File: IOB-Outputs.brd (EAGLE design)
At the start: 20.3 x 50.8 mm, 27 parts, among them CON1 CONNECTOR-IO4STD, Q1 MOSFET-N, Q10 MOSFET-P, Q11 MOSFET-P, Q12 MOSFET-P, Q2 MOSFET-N, Q3 MOSFET-N, Q4 MOSFET-N, Q5 MOSFET-N, Q6 MOSFET-N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

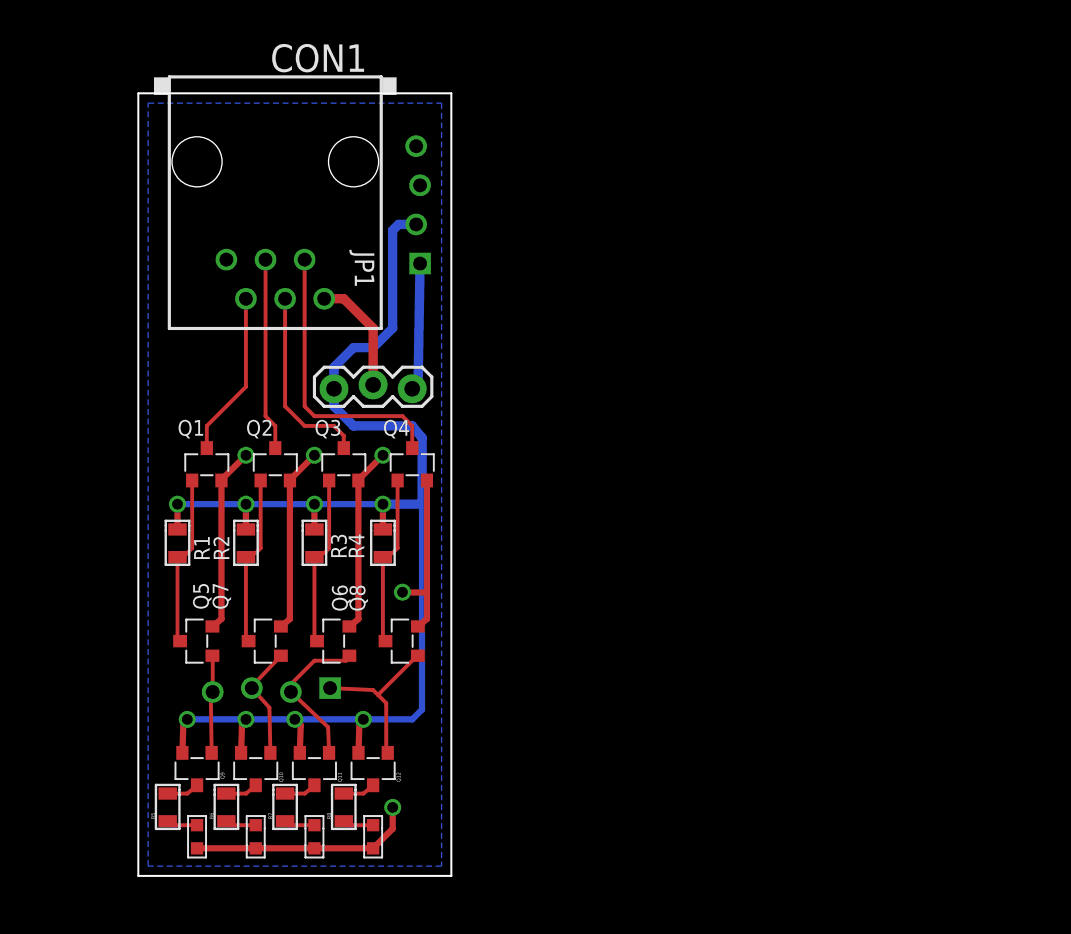
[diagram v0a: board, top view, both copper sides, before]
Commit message: updated to new IOB design
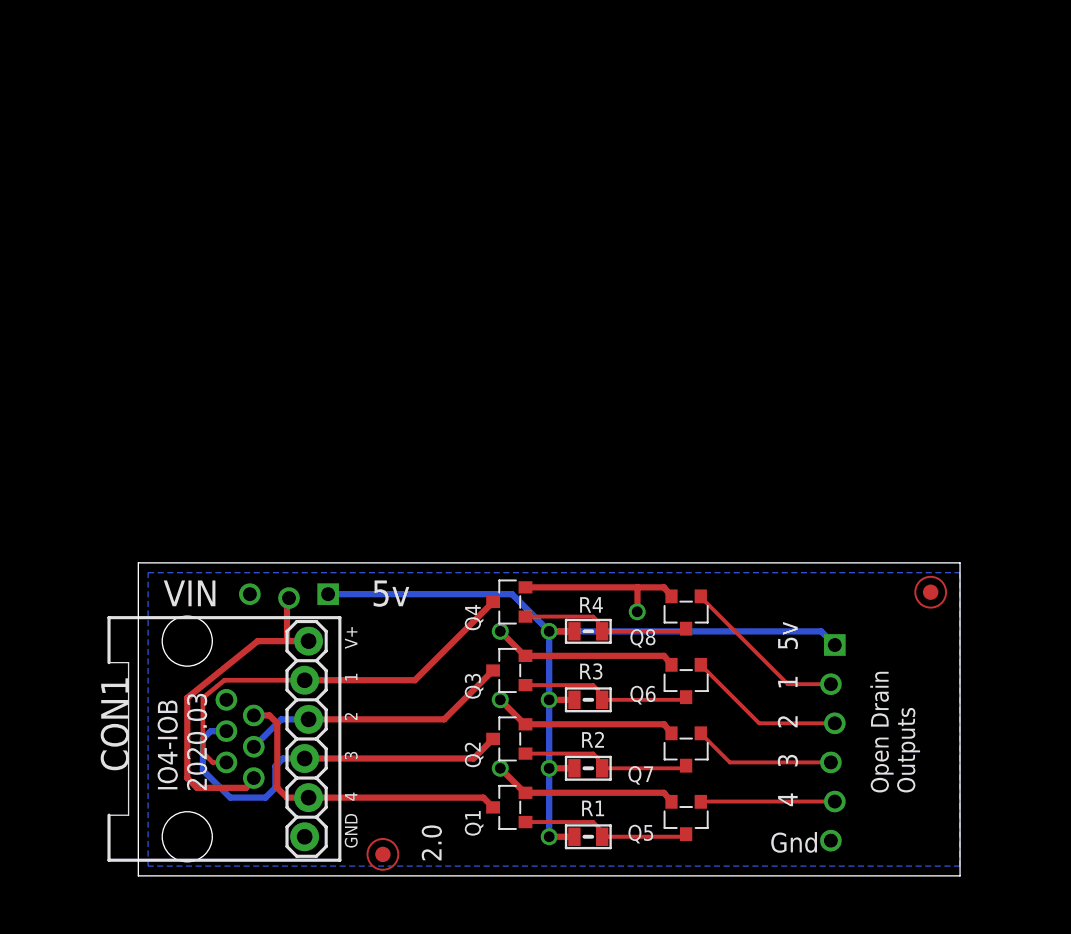
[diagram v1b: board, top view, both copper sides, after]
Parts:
- removed IOB: CONNECTOR-IO4-IOBBARE, SPCoast:IO4-IOB
- removed JP1: VIN, SPCoast:1X03
- removed LED1, LED2, LED3, LED4: Y, SPCoast:0603-LED
- removed Q10, Q11, Q12, Q9: MOSFET-P, SPCoast:SOT23-3
- removed R5, R6, R7, R8: 2K2, SPCoast:0805-RES
- added FID1, FID2: FIDUCIAL, SPCoast:FIDUCIAL_1MM
- added U$1: CONNECTOR-IO4-IOBBARE, SPCoast:IO4-IOB
- CON1: value CONNECTOR-IO4STD -> (none); device SPCoast:IO4-RJ12 -> SPCoast:RJ24-INVERTED-PINS
- moved CON1 37.5 mm to (6.99, 8.89), turned to 90 degrees
- moved Q5 33.7 mm to (35.6, 3.81), turned to 180 degrees
- moved R1 32.8 mm to (29.2, 2.54), turned to 180 degrees
- moved Q1 29.7 mm to (24.1, 4.45), turned to 90 degrees
- moved Q7 28.2 mm to (35.6, 8.26), turned to 180 degrees
- moved R2 26.6 mm to (29.2, 6.99), turned to 180 degrees
- moved Q2 23.4 mm to (24.1, 8.89), turned to 90 degrees
- moved Q6 23.0 mm to (35.6, 12.7), turned to 180 degrees
- moved R3 20.5 mm to (29.2, 11.4), turned to 180 degrees
- moved Q8 18.5 mm to (35.6, 17.1), turned to 180 degrees
- moved Q3 17.2 mm to (24.1, 13.3), turned to 90 degrees
- moved R4 14.5 mm to (29.2, 15.9), turned to 180 degrees
- moved Q4 10.9 mm to (24.1, 17.8), turned to 90 degrees
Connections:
- removed net N$11: Q12.3, R8.2
- removed net N$2: LED4.A, R8.1
- removed net N$3: LED3.A, R7.1
- removed net N$30: Q11.3, R7.2
- removed net N$31: Q10.3, R6.2
- removed net N$32: Q9.3, R5.2
- removed net N$4: LED2.A, R6.1
- removed net N$5: LED1.A, R5.1
- removed net VCCIO: CON1.1, JP1.2
- new net VOUT: CON1.1, CON1.1@1, U$1.VOUT
- net GND: now also CON1.6@1, U$1.G@3; no longer IOB.G@1, IOB.G@2, LED1.C, LED2.C, LED3.C, LED4.C
- net IO1: now also CON1.2@1
- net IO2: now also CON1.3@1
- net IO3: now also CON1.4@1
- net IO4: now also CON1.5@1
- net P1: now also U$1.P1; no longer IOB.P1, Q12.1
- net P2: now also U$1.P2; no longer IOB.P2, Q11.1
- net P3: now also U$1.P3; no longer IOB.P3, Q10.1
- net P4: now also U$1.P4; no longer IOB.P4, Q9.1
- net VCC: now also U$1.V5, U$1.V5@1; no longer IOB.V5, JP1.1, Q10.2, Q11.2, Q12.2, Q9.2
- net VIN: now also U$1.V+; no longer IOB.V+, JP1.3
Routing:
- net VCC: track 86.8 -> 54.2 mm, vias 8 -> 4
- net VOUT: track 0.00 -> 22.1 mm
- net GND: track 62.1 -> 47.5 mm, vias 5 -> 4
- net IO3: track 12.5 -> 25.7 mm
- net IO4: track 10.7 -> 20.5 mm
- net VIN: track 8.29 -> 0.00 mm
- net IO1: track 18.5 -> 26.7 mm
- net VCCIO: track 7.65 -> 0.00 mm
- net IO2: track 12.4 -> 17.6 mm
- net P4: track 6.43 -> 8.71 mm
- net N$31: track 2.11 -> 0.00 mm
- net N$32: track 2.11 -> 0.00 mm
- net N$30: track 2.11 -> 0.00 mm
- net N$11: track 2.11 -> 0.00 mm
- net N$4: track 2.01 -> 0.00 mm
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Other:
- board size 20.3 x 50.8 mm -> 53.3 x 20.3 mm
- board text added: "2020.03"
- board text added: "CON1"
- board text added: "White Soldermask Black Silkscreen"
- board text removed: "1"
- board text removed: "2"
- board text removed: "2019-11"
- board text removed: "3"
- board text removed: "4"
- board text removed: "5V"
- board text removed: "5v"
- board text removed: "IO Interface"
- board text removed: "IO4 Power"
- board text removed: "J1"
- board text removed: "JP1"
- board text removed: "Made in the PCR, Coast Div, NMRA"
- board text removed: "Model Railroading is Fun!"
- board text removed: "P1"
- board text removed: "P2"
- board text removed: "P3"
- board text removed: "P4"
- board text removed: "Q10"
- board text removed: "Q11"
- board text removed: "Q12"
- board text removed: "Q9"
- board text removed: "R5"
- board text removed: "R6"
- board text removed: "R7"
- board text removed: "R8"
- board text removed: "VIN"
- board text removed: "Vin"

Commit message: bump version
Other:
- board text added: "3.0"
- board text removed: "2.0"
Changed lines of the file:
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@@
 <setting verticaltext="up"/>
 </settings>
-<grid distance="50" unitdist="mil" unit="mil" style="dots" multiple="2" display="yes" altdistance="5" altunitdist="mil" altunit="mil"/>
+<grid distance="50" unitdist="mil" unit="mil" style="dots" multiple="2" display="yes" altdistance="25" altunitdist="mil" altunit="mil"/>
 <layers>
 <layer number="1" name="Top" color="4" fill="1" visible="yes" active="yes"/>
@@
 <wire x1="0" y1="0" x2="53.34" y2="0" width="0" layer="46"/>
 <text x="2.54" y="5.461" size="1.27" layer="21" font="vector" rot="R90">IO4-IOB</text>
-<text x="19.685" y="0.889" size="1.27" layer="21" font="vector" rot="SR90">2.0</text>
+<text x="19.685" y="0.889" size="1.27" layer="21" font="vector" rot="SR90">3.0</text>
 <text x="50.419" y="5.334" size="1.143" layer="21" font="vector" rot="R90">Open Drain
 Outputs</text>

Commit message: fixed SPCoast.lbr diode orientation
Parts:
- turned Q1 to 0 degrees
- turned Q2 to 0 degrees
- turned Q3 to 0 degrees
- turned Q4 to 0 degrees
- turned Q5 to 90 degrees
- turned Q6 to 90 degrees
- turned Q7 to 90 degrees
- turned Q8 to 90 degrees

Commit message: Added missing values
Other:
- board text added: "FID1"
- board text added: "FID2"

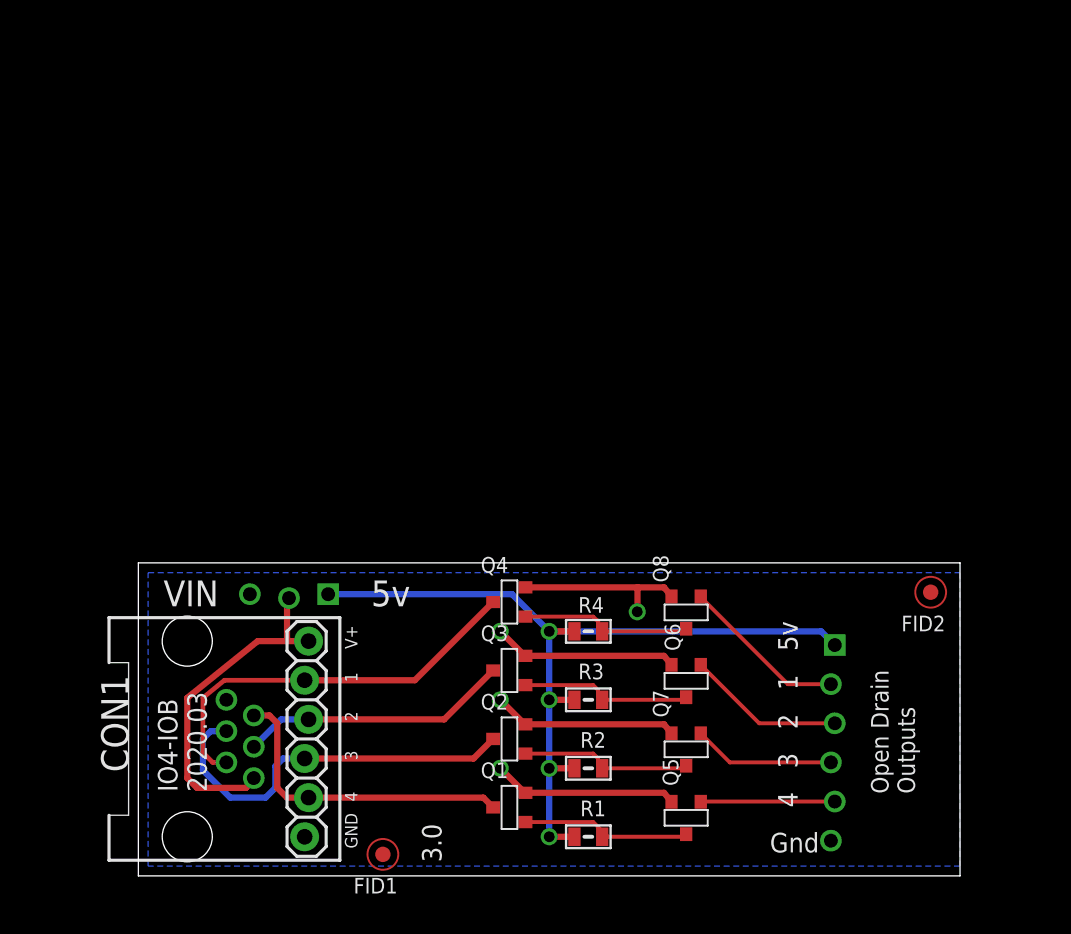
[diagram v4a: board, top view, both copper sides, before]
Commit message: normalized silkscreen layout across IOBs
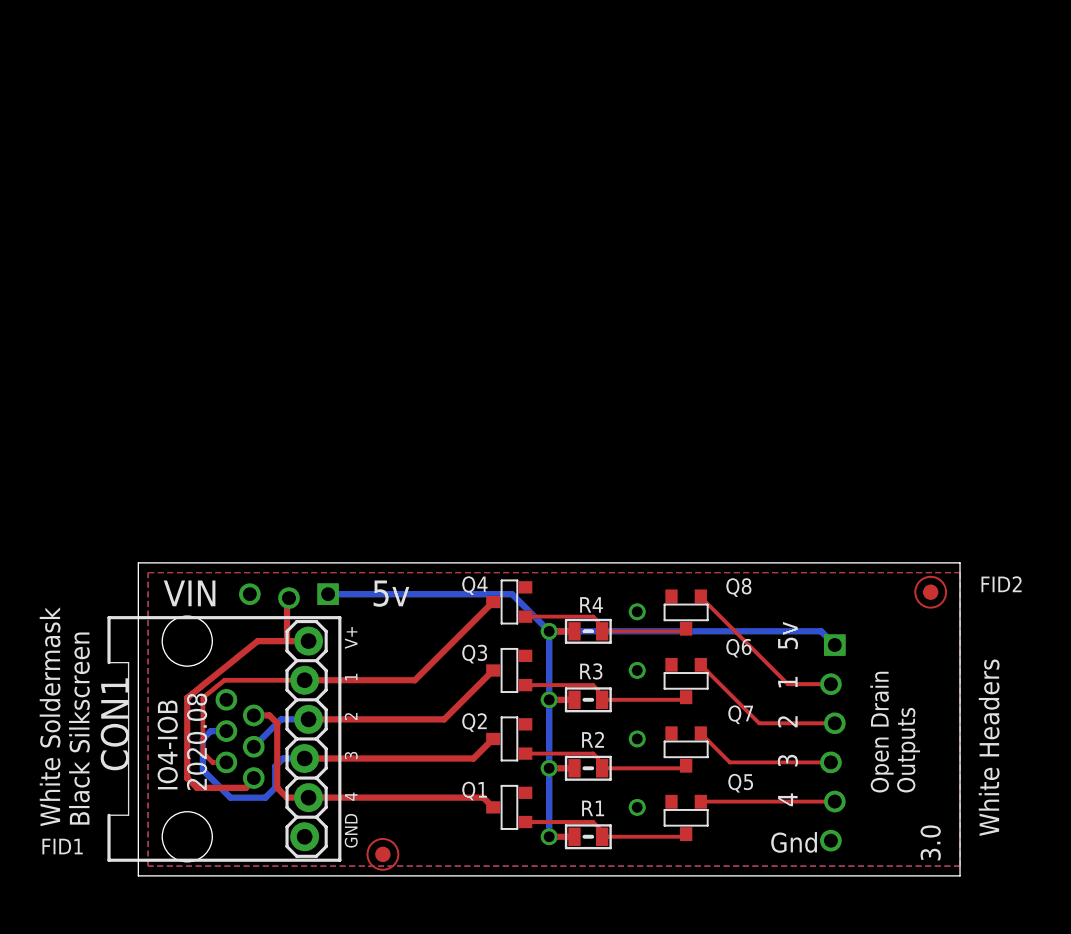
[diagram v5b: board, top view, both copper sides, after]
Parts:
- U$1: value CONNECTOR-IO4-IOBBARE -> CONNECTOR-IO4-IOBFULL
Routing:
- net GND: track 47.5 -> 0.13 mm
- added copper zone on layer 1, net GND
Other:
- board text added: "2020.08"
- board text added: "White Headers"
- board text removed: "2020.03"

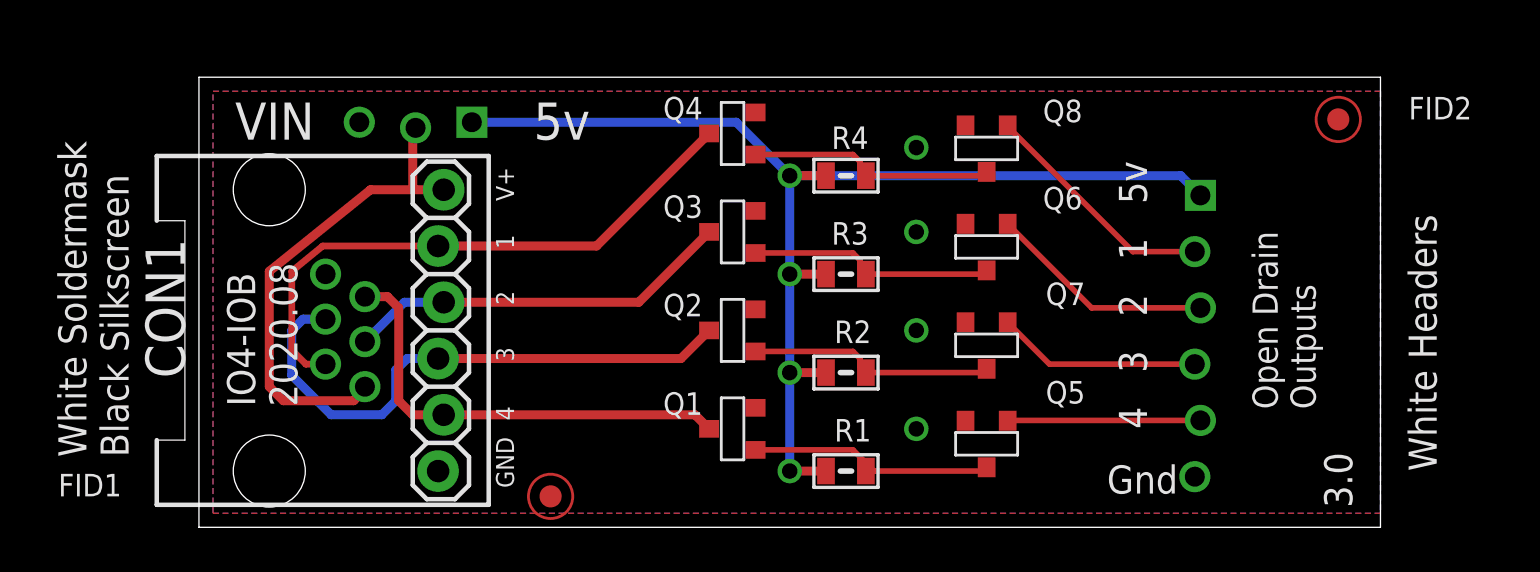
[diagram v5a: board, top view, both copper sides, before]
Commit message: move text from DOCU to TPLACE
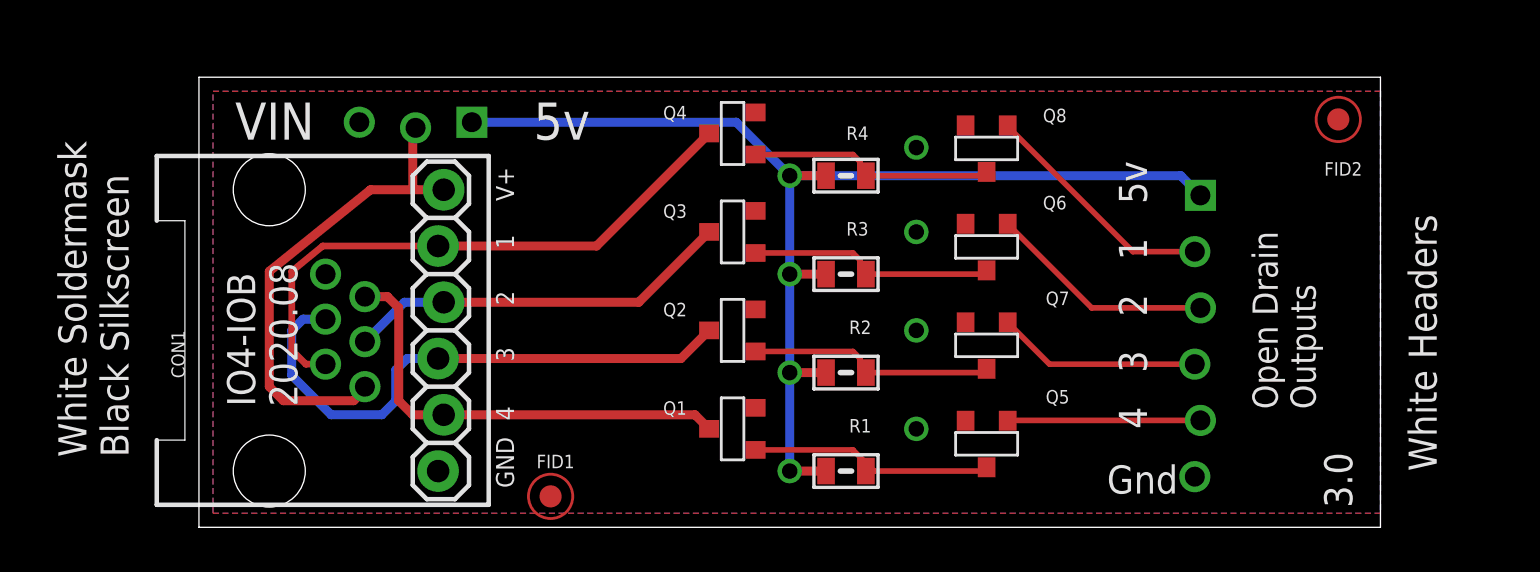
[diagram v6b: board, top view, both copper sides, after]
